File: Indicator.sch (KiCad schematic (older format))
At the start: 17 parts, among them U10 BC56-12SURKWA, U11 SC56-11SRWA, U12 MAX7219EWG+T, U8 CC56-12SURKWA, U9 MAX7219EWG+T

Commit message: Buttons complete
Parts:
- R? (x2): value 5,1K -> 47K
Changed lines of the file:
@@
 $Descr A4 11693 8268
 encoding utf-8
-Sheet 3 9
+Sheet 3 10
 Title ""
 Date ""
@@
 AR Path="/608C8099/60D74293" Ref="R?"  Part="1"
 F 0 "R?" V 9780 1900 50  0000 C CNN
-F 1 "5,1K" V 9970 1910 50  0000 C CNN
+F 1 "47K" V 9970 1910 50  0000 C CNN
 F 2 "Resistor_SMD:R_0805_2012Metric_Pad1.20x1.40mm_HandSolder" V 9800 1940 50  0001 C CNN
 F 3 "~" H 9870 1940 50  0001 C CNN
@@
 AR Path="/608C8099/60D74E3B" Ref="R?"  Part="1"
 F 0 "R?" V 8050 1890 50  0000 C CNN
-F 1 "5,1K" V 8240 1900 50  0000 C CNN
+F 1 "47K" V 8240 1900 50  0000 C CNN
 F 2 "Resistor_SMD:R_0805_2012Metric_Pad1.20x1.40mm_HandSolder" V 8070 1930 50  0001 C CNN
 F 3 "~" H 8140 1930 50  0001 C CNN

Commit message: v0.1
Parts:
- gave numbers to parts that had none: 11
- renumbered U8 to U1, U9 to U3, U10 to U4, U11 to U5, U12 to U6
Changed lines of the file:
@@
 $Descr A4 11693 8268
 encoding utf-8
-Sheet 3 9
-Title ""
-Date ""
-Rev ""
-Comp ""
-Comment1 ""
+Sheet 2 9
+Title "ШВУ"
+Date "2021-03-25"
+Rev "V0.1"
+Comp "ЦВЕТМЕТНАЛАДКА"
+Comment1 "Шустов В.И."
 Comment2 ""
 Comment3 ""
@@
 P 1880 6270
 AR Path="/608F1867" Ref="U?"  Part="1"
-AR Path="/608C8099/608F1867" Ref="U12"  Part="1"
-F 0 "U12" H 2080 7240 50  0000 C CNN
+AR Path="/608C8099/608F1867" Ref="U6"  Part="1"
+F 0 "U6" H 2080 7240 50  0000 C CNN
 F 1 "MAX7219EWG+T" H 2280 5280 50  0000 C CNN
 F 2 "Package_SO:SOIC-24W_7.5x15.4mm_P1.27mm" H 1830 6320 50  0001 C CNN
@@
 $EndComp
 $Comp
-L SVIELCOM_Library:SC56-11SRWA U11
+L SVIELCOM_Library:SC56-11SRWA U5
 U 1 1 60904CE7
 P 7590 5230
-F 0 "U11" H 7450 5800 50  0000 C CNN
+F 0 "U5" H 7450 5800 50  0000 C CNN
 F 1 "SC56-11SRWA" H 7600 4660 50  0000 C CNN
 F 2 "Display_7Segment:7SegmentLED_LTS6760_LTS6780" H 7640 4630 50  0001 C CNN
@@
 $EndComp
 $Comp
-L SVIELCOM_Library:BC56-12SURKWA U10
+L SVIELCOM_Library:BC56-12SURKWA U4
 U 1 1 60904CED
 P 5320 5230
-F 0 "U10" H 4380 6140 50  0000 C CNN
+F 0 "U4" H 4380 6140 50  0000 C CNN
 F 1 "BC56-12SURKWA" H 4640 6050 50  0000 C CNN
 F 2 "SVIELCOM:BC56-11SURKWA" H 5370 4330 50  0001 C CNN
@@
 $EndComp
 $Comp
-L SVIELCOM_Library:CC56-12SURKWA U8
+L SVIELCOM_Library:CC56-12SURKWA U1
 U 1 1 60904CF3
 P 5320 1750
-F 0 "U8" H 4370 2390 50  0000 C CNN
+F 0 "U1" H 4370 2390 50  0000 C CNN
 F 1 "CC56-12SURKWA" H 4640 2310 50  0000 C CNN
 F 2 "Display_7Segment:CA56-12SURKWA" H 5320 1150 50  0001 C CNN
@@
 $EndComp
 $Comp
-L SVIELCOM_Library:CC56-12SURKWA U?
+L SVIELCOM_Library:CC56-12SURKWA U2
 U 1 1 60A2DE5F
 P 5320 2950
-F 0 "U?" H 4370 3590 50  0000 C CNN
+F 0 "U2" H 4370 3590 50  0000 C CNN
 F 1 "CC56-12SURKWA" H 4640 3510 50  0000 C CNN
 F 2 "Display_7Segment:CA56-12SURKWA" H 5320 2350 50  0001 C CNN
@@
 "Вес"
 $Comp
-L SVIELCOM_Library:CC56-12SURKWA U?
+L SVIELCOM_Library:CC56-12SURKWA U7
 U 1 1 60A5D5C4
 P 5320 7120
-F 0 "U?" H 4370 7760 50  0000 C CNN
+F 0 "U7" H 4370 7760 50  0000 C CNN
 F 1 "CC56-12SURKWA" H 4640 7680 50  0000 C CNN
 F 2 "Display_7Segment:CA56-12SURKWA" H 5320 6520 50  0001 C CNN
@@
 AR Path="/60C51BAE" Ref="R?"  Part="1"
 AR Path="/60A03F8A/60C51BAE" Ref="R?"  Part="1"
-AR Path="/608C8099/60C51BAE" Ref="R?"  Part="1"
-F 0 "R?" H 1580 5330 50  0000 C CNN
+AR Path="/608C8099/60C51BAE" Ref="R6"  Part="1"
+F 0 "R6" H 1580 5330 50  0000 C CNN
 F 1 "17,1K" H 1640 5240 50  0000 C CNN
 F 2 "Resistor_SMD:R_0805_2012Metric_Pad1.20x1.40mm_HandSolder" V 1390 5250 50  0001 C CNN
@@
 $EndComp
 $Comp
-L SVIELCOM_Library:+5V #PWR?
+L SVIELCOM_Library:+5V #PWR07
 U 1 1 60C625DC
 P 1880 4950
-F 0 "#PWR?" H 1880 4800 50  0001 C CNN
+F 0 "#PWR07" H 1880 4800 50  0001 C CNN
 F 1 "+5V" H 1895 5123 50  0000 C CNN
 F 2 "" H 1880 4950 50  0001 C CNN
@@
 AR Path="/60C90DD1" Ref="R?"  Part="1"
 AR Path="/60A03F8A/60C90DD1" Ref="R?"  Part="1"
-AR Path="/608C8099/60C90DD1" Ref="R?"  Part="1"
-F 0 "R?" H 1570 2030 50  0000 C CNN
+AR Path="/608C8099/60C90DD1" Ref="R5"  Part="1"
+F 0 "R5" H 1570 2030 50  0000 C CNN
 F 1 "17,1K" H 1630 1940 50  0000 C CNN
 F 2 "Resistor_SMD:R_0805_2012Metric_Pad1.20x1.40mm_HandSolder" V 1380 1950 50  0001 C CNN
@@
 	1450 1720 1880 1720
 $Comp
-L SVIELCOM_Library:+5V #PWR?
+L SVIELCOM_Library:+5V #PWR03
 U 1 1 60C9A9E7
 P 1880 1650
-F 0 "#PWR?" H 1880 1500 50  0001 C CNN
+F 0 "#PWR03" H 1880 1500 50  0001 C CNN
 F 1 "+5V" H 1895 1823 50  0000 C CNN
 F 2 "" H 1880 1650 50  0001 C CNN
@@
 P 1880 2970
 AR Path="/608F051E" Ref="U?"  Part="1"
-AR Path="/608C8099/608F051E" Ref="U9"  Part="1"
-F 0 "U9" H 2070 3920 50  0000 C CNN
+AR Path="/608C8099/608F051E" Ref="U3"  Part="1"
+F 0 "U3" H 2070 3920 50  0000 C CNN
 F 1 "MAX7219EWG+T" H 1250 2810 50  0000 C CNN
 F 2 "Package_SO:SOIC-24W_7.5x15.4mm_P1.27mm" H 1830 3020 50  0001 C CNN
@@
 AR Path="/60CD686B" Ref="#PWR?"  Part="1"
 AR Path="/60A03F8A/60CD686B" Ref="#PWR?"  Part="1"
-AR Path="/608C8099/60CD686B" Ref="#PWR?"  Part="1"
-F 0 "#PWR?" H 1880 3830 50  0001 C CNN
+AR Path="/608C8099/60CD686B" Ref="#PWR06"  Part="1"
+F 0 "#PWR06" H 1880 3830 50  0001 C CNN
 F 1 "GNDREF" V 1885 3952 50  0001 R CNN
 F 2 "" H 1880 4080 50  0001 C CNN
@@
 AR Path="/60CE9A00" Ref="#PWR?"  Part="1"
 AR Path="/60A03F8A/60CE9A00" Ref="#PWR?"  Part="1"
-AR Path="/608C8099/60CE9A00" Ref="#PWR?"  Part="1"
-F 0 "#PWR?" H 1880 7130 50  0001 C CNN
+AR Path="/608C8099/60CE9A00" Ref="#PWR08"  Part="1"
+F 0 "#PWR08" H 1880 7130 50  0001 C CNN
 F 1 "GNDREF" V 1885 7252 50  0001 R CNN
 F 2 "" H 1880 7380 50  0001 C CNN
@@
 PG14
 $Comp
-L Device:LED D?
+L Device:LED D1
 U 1 1 60D12378
 P 8590 1480
-F 0 "D?" V 8650 1340 50  0000 C CNN
+F 0 "D1" V 8650 1340 50  0000 C CNN
 F 1 "L-1154ID" V 8560 1200 50  0000 C CNN
 F 2 "LED_THT:LED_D3.0mm" H 8590 1480 50  0001 C CNN
@@
 $EndComp
 $Comp
-L dk_Transistors-Bipolar-BJT-Single:BC817-25LT1G Q?
+L dk_Transistors-Bipolar-BJT-Single:BC817-25LT1G Q1
 U 1 1 60D173AB
 P 8490 1930
-F 0 "Q?" H 8320 2110 60  0000 L CNN
+F 0 "Q1" H 8320 2110 60  0000 L CNN
 F 1 "BC817-25LT1G" H 7840 1710 60  0000 L CNN
 F 2 "digikey-footprints:SOT-23-3" H 8690 2130 60  0001 L CNN
@@
 $EndComp
 $Comp
-L dk_Transistors-Bipolar-BJT-Single:BC817-25LT1G Q?
+L dk_Transistors-Bipolar-BJT-Single:BC817-25LT1G Q2
 U 1 1 60D194A1
 P 10220 1940
-F 0 "Q?" H 9930 1780 60  0000 L CNN
+F 0 "Q2" H 9930 1780 60  0000 L CNN
 F 1 "BC817-25LT1G" H 9570 1700 60  0000 L CNN
 F 2 "digikey-footprints:SOT-23-3" H 10420 2140 60  0001 L CNN
@@
 AR Path="/60D3CAE8" Ref="R?"  Part="1"
 AR Path="/60A03F8A/60D3CAE8" Ref="R?"  Part="1"
-AR Path="/608C8099/60D3CAE8" Ref="R?"  Part="1"
-F 0 "R?" H 8710 1160 50  0000 C CNN
+AR Path="/608C8099/60D3CAE8" Ref="R1"  Part="1"
+F 0 "R1" H 8710 1160 50  0000 C CNN
 F 1 "100" H 8730 1070 50  0000 C CNN
 F 2 "Resistor_SMD:R_0805_2012Metric_Pad1.20x1.40mm_HandSolder" V 8520 1080 50  0001 C CNN
@@
 AR Path="/60D3D796" Ref="R?"  Part="1"
 AR Path="/60A03F8A/60D3D796" Ref="R?"  Part="1"
-AR Path="/608C8099/60D3D796" Ref="R?"  Part="1"
-F 0 "R?" H 10440 1170 50  0000 C CNN
+AR Path="/608C8099/60D3D796" Ref="R2"  Part="1"
+F 0 "R2" H 10440 1170 50  0000 C CNN
 F 1 "100" H 10450 1080 50  0000 C CNN
 F 2 "Resistor_SMD:R_0805_2012Metric_Pad1.20x1.40mm_HandSolder" V 10250 1090 50  0001 C CNN
@@
 AR Path="/60D66B48" Ref="#PWR?"  Part="1"
 AR Path="/60A03F8A/60D66B48" Ref="#PWR?"  Part="1"
-AR Path="/608C8099/60D66B48" Ref="#PWR?"  Part="1"
-F 0 "#PWR?" H 10320 1950 50  0001 C CNN
+AR Path="/608C8099/60D66B48" Ref="#PWR05"  Part="1"
+F 0 "#PWR05" H 10320 1950 50  0001 C CNN
 F 1 "GNDREF" V 10325 2072 50  0001 R CNN
 F 2 "" H 10320 2200 50  0001 C CNN
@@
 $EndComp
 $Comp
-L SVIELCOM_Library:+5V #PWR?
+L SVIELCOM_Library:+5V #PWR02
 U 1 1 60D69A05
 P 10320 890
-F 0 "#PWR?" H 10320 740 50  0001 C CNN
+F 0 "#PWR02" H 10320 740 50  0001 C CNN
 F 1 "+5V" H 10335 1063 50  0000 C CNN
 F 2 "" H 10320 890 50  0001 C CNN
@@
 AR Path="/60D74293" Ref="R?"  Part="1"
 AR Path="/60A03F8A/60D74293" Ref="R?"  Part="1"
-AR Path="/608C8099/60D74293" Ref="R?"  Part="1"
-F 0 "R?" V 9780 1900 50  0000 C CNN
+AR Path="/608C8099/60D74293" Ref="R4"  Part="1"
+F 0 "R4" V 9780 1900 50  0000 C CNN
 F 1 "47K" V 9970 1910 50  0000 C CNN
 F 2 "Resistor_SMD:R_0805_2012Metric_Pad1.20x1.40mm_HandSolder" V 9800 1940 50  0001 C CNN
@@
 AR Path="/60D74E3B" Ref="R?"  Part="1"
 AR Path="/60A03F8A/60D74E3B" Ref="R?"  Part="1"
-AR Path="/608C8099/60D74E3B" Ref="R?"  Part="1"
-F 0 "R?" V 8050 1890 50  0000 C CNN
+AR Path="/608C8099/60D74E3B" Ref="R3"  Part="1"
+F 0 "R3" V 8050 1890 50  0000 C CNN
 F 1 "47K" V 8240 1900 50  0000 C CNN
 F 2 "Resistor_SMD:R_0805_2012Metric_Pad1.20x1.40mm_HandSolder" V 8070 1930 50  0001 C CNN
@@
 $EndComp
 $Comp
-L SVIELCOM_Library:+5V #PWR?
+L SVIELCOM_Library:+5V #PWR01
 U 1 1 60D8BCE0
 P 8590 890
-F 0 "#PWR?" H 8590 740 50  0001 C CNN
+F 0 "#PWR01" H 8590 740 50  0001 C CNN
 F 1 "+5V" H 8605 1063 50  0000 C CNN
 F 2 "" H 8590 890 50  0001 C CNN
@@
 AR Path="/60DA0F1A" Ref="#PWR?"  Part="1"
 AR Path="/60A03F8A/60DA0F1A" Ref="#PWR?"  Part="1"
-AR Path="/608C8099/60DA0F1A" Ref="#PWR?"  Part="1"
-F 0 "#PWR?" H 8590 1940 50  0001 C CNN
+AR Path="/608C8099/60DA0F1A" Ref="#PWR04"  Part="1"
+F 0 "#PWR04" H 8590 1940 50  0001 C CNN
 F 1 "GNDREF" V 8595 2062 50  0001 R CNN
 F 2 "" H 8590 2190 50  0001 C CNN

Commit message: footprints associations is done
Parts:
- removed R6: 17,1K, Resistor_SMD:R_0805_2012Metric_Pad1.20x1.40mm_HandSolder, symbol Device:R
- added R3, R7: 200, Resistor_SMD:R_0805_2012Metric_Pad1.20x1.40mm_HandSolder, symbol Device:R
- added R8: 16,9K, Resistor_SMD:R_0805_2012Metric_Pad1.20x1.40mm_HandSolder, symbol Device:R
- added TP1, TP2, TP3, TP4: TestPoint, TestPoint:TestPoint_Pad_D1.5mm, symbol Connector:TestPoint
- R6: renamed from R5; value 17,1K -> 16,9K; Order (none) -> RC0805FR-0716K9L
- renumbered R3 to R4, R4 to R5
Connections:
- net +5V: now also R3.1, R7.1; no longer R6.1
- net SPI6_CS: now also TP2.1
- net SPI6_MOSI: now also TP1.1
- net SPI6_SCK: now also TP3.1
- net at U3.24 (DOUT), U6.1 (DIN): now also TP4.1
- net at U6.18 (ISET): now also R8.2
- new net: R3.2, R6.1
- new net: R7.2, R8.1
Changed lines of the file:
@@
 Title "ШВУ"
 Date "2021-03-25"
-Rev "V0.1"
+Rev "V0.3"
 Comp "ЦВЕТМЕТНАЛАДКА"
 Comment1 "Шустов В.И."
@@
 	2410 3770 2410 4470
 Wire Wire Line
-	2410 4470 1350 4470
+	2410 4470 1540 4470
 Wire Wire Line
 	1350 4470 1350 7070
@@
 	1480 6970 1220 6970
 Wire Wire Line
-	1220 6970 1220 3670
+	1220 6970 1220 4140
 Wire Wire Line
 	1220 3670 1480 3670
@@
 	1480 6870 1080 6870
 Wire Wire Line
-	1080 6870 1080 3570
+	1080 6870 1080 4140
 Wire Wire Line
 	1080 3570 1480 3570
-$Comp
-L Device:R R?
-U 1 1 60C51BAE
-P 1460 5250
-AR Path="/60C51BAE" Ref="R?"  Part="1"
-AR Path="/60A03F8A/60C51BAE" Ref="R?"  Part="1"
-AR Path="/608C8099/60C51BAE" Ref="R6"  Part="1"
-F 0 "R6" H 1580 5330 50  0000 C CNN
-F 1 "17,1K" H 1640 5240 50  0000 C CNN
-F 2 "Resistor_SMD:R_0805_2012Metric_Pad1.20x1.40mm_HandSolder" V 1390 5250 50  0001 C CNN
-F 3 "~" H 1460 5250 50  0001 C CNN
-	1    1460 5250
-	1    0    0    -1
-$EndComp
 $Comp
 L SVIELCOM_Library:+5V #PWR07
@@
 Wire Wire Line
 	1460 5470 1480 5470
-Wire Wire Line
-	1880 4950 1880 5020
-Wire Wire Line
-	1460 5100 1460 5020
-Wire Wire Line
-	1460 5020 1880 5020
-Connection ~ 1880 5020
-Wire Wire Line
-	1880 5020 1880 5270
 $Comp
 L Device:R R?
@@
 AR Path="/60C90DD1" Ref="R?"  Part="1"
 AR Path="/60A03F8A/60C90DD1" Ref="R?"  Part="1"
-AR Path="/608C8099/60C90DD1" Ref="R5"  Part="1"
-F 0 "R5" H 1570 2030 50  0000 C CNN
-F 1 "17,1K" H 1630 1940 50  0000 C CNN
+AR Path="/608C8099/60C90DD1" Ref="R6"  Part="1"
+F 0 "R6" H 1320 2040 50  0000 C CNN
+F 1 "16,9K" H 1280 1940 50  0000 C CNN
 F 2 "Resistor_SMD:R_0805_2012Metric_Pad1.20x1.40mm_HandSolder" V 1380 1950 50  0001 C CNN
 F 3 "~" H 1450 1950 50  0001 C CNN
+F 4 "RC0805FR-0716K9L" H 1450 1950 50  0001 C CNN "Order"
 	1    1450 1950
 	1    0    0    -1
 $EndComp
-Wire Wire Line
-	1450 1800 1450 1720
-Wire Wire Line
-	1450 1720 1880 1720
 $Comp
 L SVIELCOM_Library:+5V #PWR03
@@
 	1    0    0    -1
 $EndComp
-Wire Wire Line
-	1880 1650 1880 1720
 $Comp
 L Driver_LED:MAX7219 U?
@@
 Wire Wire Line
 	1450 2170 1480 2170
-Wire Wire Line
-	1880 1970 1880 1720
-Connection ~ 1880 1720
 NoConn ~ 2280 7070
 $Comp
@@
 SPI6_MOSI
 Wire Wire Line
-	980  3770 1480 3770
+	980  3770 1450 3770
 Text Label 1240 3670 0    50   ~ 0
 PG13
@@
 AR Path="/60D74293" Ref="R?"  Part="1"
 AR Path="/60A03F8A/60D74293" Ref="R?"  Part="1"
-AR Path="/608C8099/60D74293" Ref="R4"  Part="1"
-F 0 "R4" V 9780 1900 50  0000 C CNN
+AR Path="/608C8099/60D74293" Ref="R5"  Part="1"
+F 0 "R5" V 9780 1900 50  0000 C CNN
 F 1 "47K" V 9970 1910 50  0000 C CNN
 F 2 "Resistor_SMD:R_0805_2012Metric_Pad1.20x1.40mm_HandSolder" V 9800 1940 50  0001 C CNN
@@
 AR Path="/60D74E3B" Ref="R?"  Part="1"
 AR Path="/60A03F8A/60D74E3B" Ref="R?"  Part="1"
-AR Path="/608C8099/60D74E3B" Ref="R3"  Part="1"
-F 0 "R3" V 8050 1890 50  0000 C CNN
+AR Path="/608C8099/60D74E3B" Ref="R4"  Part="1"
+F 0 "R4" V 8050 1890 50  0000 C CNN
 F 1 "47K" V 8240 1900 50  0000 C CNN
 F 2 "Resistor_SMD:R_0805_2012Metric_Pad1.20x1.40mm_HandSolder" V 8070 1930 50  0001 C CNN
@@
 Text Notes 10460 1640 0    50   ~ 0
 "EAST"
+Wire Wire Line
+	1880 1650 1880 1720
+$Comp
+L Device:R R?
+U 1 1 618A3C48
+P 1670 1720
+AR Path="/618A3C48" Ref="R?"  Part="1"
+AR Path="/60A03F8A/618A3C48" Ref="R?"  Part="1"
+AR Path="/608C8099/618A3C48" Ref="R3"  Part="1"
+F 0 "R3" V 1560 1610 50  0000 C CNN
+F 1 "200" V 1560 1800 50  0000 C CNN
+F 2 "Resistor_SMD:R_0805_2012Metric_Pad1.20x1.40mm_HandSolder" V 1600 1720 50  0001 C CNN
+F 3 "~" H 1670 1720 50  0001 C CNN
+F 4 "ERJ6ENF2000V" H 1670 1720 50  0001 C CNN "Order"
+	1    1670 1720
+	0    1    1    0
+$EndComp
+Wire Wire Line
+	1450 1800 1450 1720
+Wire Wire Line
+	1450 1720 1520 1720
+Wire Wire Line
+	1820 1720 1880 1720
+Connection ~ 1880 1720
+Wire Wire Line
+	1880 1720 1880 1970
+Wire Wire Line
+	1880 4950 1880 5020
+$Comp
+L Device:R R?
+U 1 1 618BA407
+P 1460 5250
+AR Path="/618BA407" Ref="R?"  Part="1"
+AR Path="/60A03F8A/618BA407" Ref="R?"  Part="1"
+AR Path="/608C8099/618BA407" Ref="R8"  Part="1"
+F 0 "R8" H 1570 5320 50  0000 C CNN
+F 1 "16,9K" H 1620 5240 50  0000 C CNN
+F 2 "Resistor_SMD:R_0805_2012Metric_Pad1.20x1.40mm_HandSolder" V 1390 5250 50  0001 C CNN
+F 3 "~" H 1460 5250 50  0001 C CNN
+F 4 "RC0805FR-0716K9L" H 1460 5250 50  0001 C CNN "Order"
+	1    1460 5250
+	1    0    0    -1
+$EndComp
+$Comp
+L Device:R R?
+U 1 1 618BA40E
+P 1680 5020
+AR Path="/618BA40E" Ref="R?"  Part="1"
+AR Path="/60A03F8A/618BA40E" Ref="R?"  Part="1"
+AR Path="/608C8099/618BA40E" Ref="R7"  Part="1"
+F 0 "R7" V 1570 4910 50  0000 C CNN
+F 1 "200" V 1570 5100 50  0000 C CNN
+F 2 "Resistor_SMD:R_0805_2012Metric_Pad1.20x1.40mm_HandSolder" V 1610 5020 50  0001 C CNN
+F 3 "~" H 1680 5020 50  0001 C CNN
+F 4 "ERJ6ENF2000V" H 1680 5020 50  0001 C CNN "Order"
+	1    1680 5020
+	0    1    1    0
+$EndComp
+Wire Wire Line
+	1460 5100 1460 5020
+Wire Wire Line
+	1460 5020 1530 5020
+Wire Wire Line
+	1830 5020 1880 5020
+Connection ~ 1880 5020
+Wire Wire Line
+	1880 5020 1880 5270
+$Comp
+L Connector:TestPoint TP?
+U 1 1 61C03EE6
+P 1540 4470
+AR Path="/60D8C564/61C03EE6" Ref="TP?"  Part="1"
+AR Path="/608C8099/61C03EE6" Ref="TP4"  Part="1"
+F 0 "TP4" H 1490 4680 50  0000 L CNN
+F 1 "TestPoint" H 1600 4670 50  0001 L CNN
+F 2 "TestPoint:TestPoint_Pad_D1.5mm" H 1740 4470 50  0001 C CNN
+F 3 "~" H 1740 4470 50  0001 C CNN
+	1    1540 4470
+	1    0    0    -1
+$EndComp
+Connection ~ 1540 4470
+Wire Wire Line
+	1540 4470 1350 4470
+$Comp
+L Connector:TestPoint TP?
+U 1 1 61C0EE07
+P 1080 4140
+AR Path="/60D8C564/61C0EE07" Ref="TP?"  Part="1"
+AR Path="/608C8099/61C0EE07" Ref="TP2"  Part="1"
+F 0 "TP2" H 1030 4350 50  0000 L CNN
+F 1 "TestPoint" H 1140 4340 50  0001 L CNN
+F 2 "TestPoint:TestPoint_Pad_D1.5mm" H 1280 4140 50  0001 C CNN
+F 3 "~" H 1280 4140 50  0001 C CNN
+	1    1080 4140
+	0    -1   -1   0
+$EndComp
+$Comp
+L Connector:TestPoint TP?
+U 1 1 61C19E94
+P 1220 4140
+AR Path="/60D8C564/61C19E94" Ref="TP?"  Part="1"
+AR Path="/608C8099/61C19E94" Ref="TP3"  Part="1"
+F 0 "TP3" H 1170 4350 50  0000 L CNN
+F 1 "TestPoint" H 1280 4340 50  0001 L CNN
+F 2 "TestPoint:TestPoint_Pad_D1.5mm" H 1420 4140 50  0001 C CNN
+F 3 "~" H 1420 4140 50  0001 C CNN
+	1    1220 4140
+	0    1    1    0
+$EndComp
 Wire Bus Line
 	2550 690  6810 690
@@
 Wire Bus Line
 	2550 690  2550 3570
+Connection ~ 1220 4140
+Wire Wire Line
+	1220 4140 1220 3670
+Connection ~ 1080 4140
+Wire Wire Line
+	1080 4140 1080 3570
+$Comp
+L Connector:TestPoint TP?
+U 1 1 61C24CDA
+P 1450 3770
+AR Path="/60D8C564/61C24CDA" Ref="TP?"  Part="1"
+AR Path="/608C8099/61C24CDA" Ref="TP1"  Part="1"
+F 0 "TP1" H 1400 3980 50  0000 L CNN
+F 1 "TestPoint" H 1510 3970 50  0001 L CNN
+F 2 "TestPoint:TestPoint_Pad_D1.5mm" H 1650 3770 50  0001 C CNN
+F 3 "~" H 1650 3770 50  0001 C CNN
+	1    1450 3770
+	-1   0    0    1
+$EndComp
+Connection ~ 1450 3770
+Wire Wire Line
+	1450 3770 1480 3770
 $EndSCHEMATC

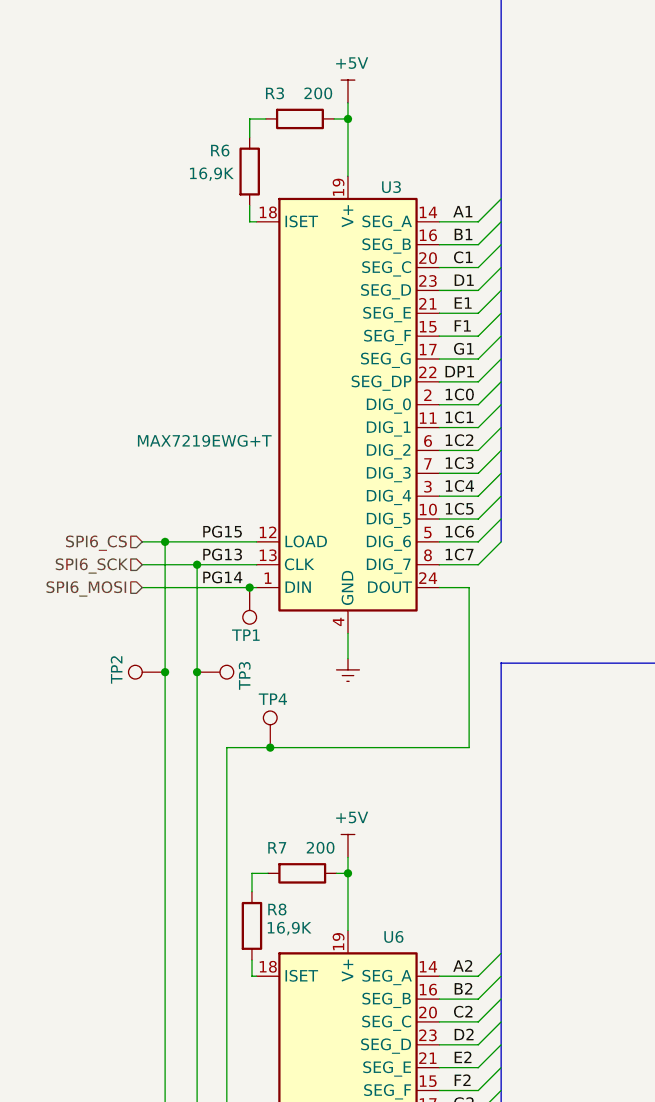
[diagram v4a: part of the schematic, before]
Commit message: corrected few footprints, correct all resistors and capacitors type for ordering
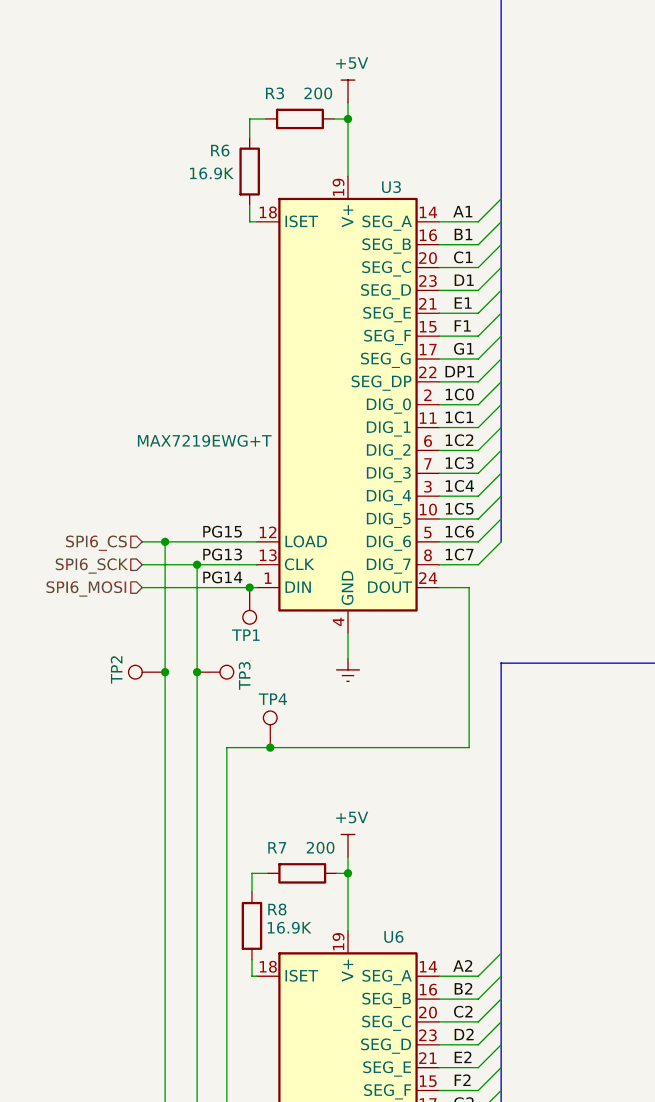
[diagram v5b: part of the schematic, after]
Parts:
- R1, R2: Type (none) -> RC0805FR-07100RL
- R3, R7: Order ERJ6ENF2000V -> (none); Type (none) -> ERJ6ENF2000V
- R4, R5: Type (none) -> RC0805FR-0747KL
- R6, R8: value 16,9K -> 16.9K; Order RC0805FR-0716K9L -> (none); Type (none) -> RC0805FR-0716K9L
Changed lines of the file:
@@
 AR Path="/608C8099/60C90DD1" Ref="R6"  Part="1"
 F 0 "R6" H 1320 2040 50  0000 C CNN
-F 1 "16,9K" H 1280 1940 50  0000 C CNN
+F 1 "16.9K" H 1280 1940 50  0000 C CNN
 F 2 "Resistor_SMD:R_0805_2012Metric_Pad1.20x1.40mm_HandSolder" V 1380 1950 50  0001 C CNN
 F 3 "~" H 1450 1950 50  0001 C CNN
-F 4 "RC0805FR-0716K9L" H 1450 1950 50  0001 C CNN "Order"
+F 4 "RC0805FR-0716K9L" H 1450 1950 50  0001 C CNN "Type"
 	1    1450 1950
 	1    0    0    -1
@@
 F 2 "Resistor_SMD:R_0805_2012Metric_Pad1.20x1.40mm_HandSolder" V 8520 1080 50  0001 C CNN
 F 3 "~" H 8590 1080 50  0001 C CNN
+F 4 "RC0805FR-07100RL" H 8590 1080 50  0001 C CNN "Type"
 	1    8590 1080
 	1    0    0    -1
@@
 F 2 "Resistor_SMD:R_0805_2012Metric_Pad1.20x1.40mm_HandSolder" V 10250 1090 50  0001 C CNN
 F 3 "~" H 10320 1090 50  0001 C CNN
+F 4 "RC0805FR-07100RL" H 10320 1090 50  0001 C CNN "Type"
 	1    10320 1090
 	1    0    0    -1
@@
 F 2 "Resistor_SMD:R_0805_2012Metric_Pad1.20x1.40mm_HandSolder" V 9800 1940 50  0001 C CNN
 F 3 "~" H 9870 1940 50  0001 C CNN
+F 4 "RC0805FR-0747KL" V 9870 1940 50  0001 C CNN "Type"
 	1    9870 1940
 	0    1    1    0
@@
 F 2 "Resistor_SMD:R_0805_2012Metric_Pad1.20x1.40mm_HandSolder" V 8070 1930 50  0001 C CNN
 F 3 "~" H 8140 1930 50  0001 C CNN
+F 4 "RC0805FR-0747KL" V 8140 1930 50  0001 C CNN "Type"
 	1    8140 1930
 	0    1    1    0
@@
 F 2 "Resistor_SMD:R_0805_2012Metric_Pad1.20x1.40mm_HandSolder" V 1600 1720 50  0001 C CNN
 F 3 "~" H 1670 1720 50  0001 C CNN
-F 4 "ERJ6ENF2000V" H 1670 1720 50  0001 C CNN "Order"
+F 4 "ERJ6ENF2000V" H 1670 1720 50  0001 C CNN "Type"
 	1    1670 1720
 	0    1    1    0
@@
 AR Path="/608C8099/618BA407" Ref="R8"  Part="1"
 F 0 "R8" H 1570 5320 50  0000 C CNN
-F 1 "16,9K" H 1620 5240 50  0000 C CNN
+F 1 "16.9K" H 1620 5240 50  0000 C CNN
 F 2 "Resistor_SMD:R_0805_2012Metric_Pad1.20x1.40mm_HandSolder" V 1390 5250 50  0001 C CNN
 F 3 "~" H 1460 5250 50  0001 C CNN
-F 4 "RC0805FR-0716K9L" H 1460 5250 50  0001 C CNN "Order"
+F 4 "RC0805FR-0716K9L" H 1460 5250 50  0001 C CNN "Type"
 	1    1460 5250
 	1    0    0    -1
@@
 F 2 "Resistor_SMD:R_0805_2012Metric_Pad1.20x1.40mm_HandSolder" V 1610 5020 50  0001 C CNN
 F 3 "~" H 1680 5020 50  0001 C CNN
-F 4 "ERJ6ENF2000V" H 1680 5020 50  0001 C CNN "Order"
+F 4 "ERJ6ENF2000V" H 1680 5020 50  0001 C CNN "Type"
 	1    1680 5020
 	0    1    1    0
